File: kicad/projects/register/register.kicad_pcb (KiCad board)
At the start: 2 copper layers, 215.9 x 129.5 mm, 21 parts, among them J1 LEFT IN, J10 RIGHT LEDS, J2 LEFT OUT, J3 LEFT CONTENT, J4 BUS, J5 LEFT LEDS, J6 BACKPLANE, J7 RIGHT IN, J8 RIGHT OUT, J9 RIGHT CONTENT, U1 74HCT377, U2 74HCT245, U3 74HCT04, U4 74HCT377, U5 74HCT245

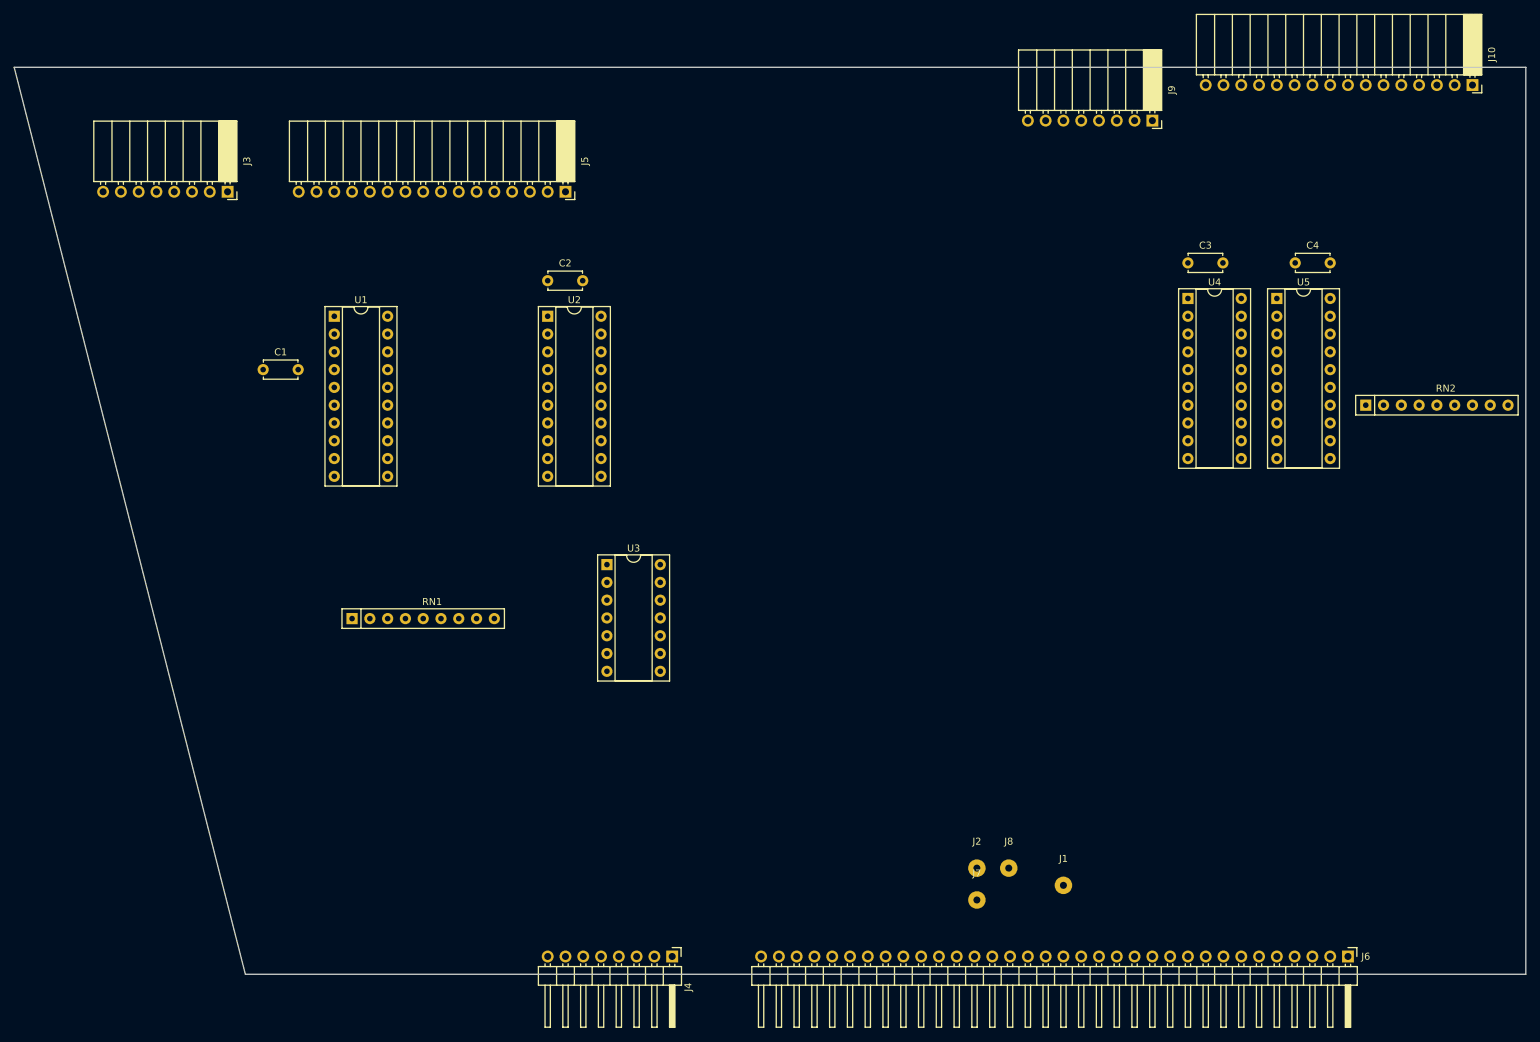
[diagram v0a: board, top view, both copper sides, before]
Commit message: Add start of control unit in kicad. Start routing register PCB, need to make traces thinner...
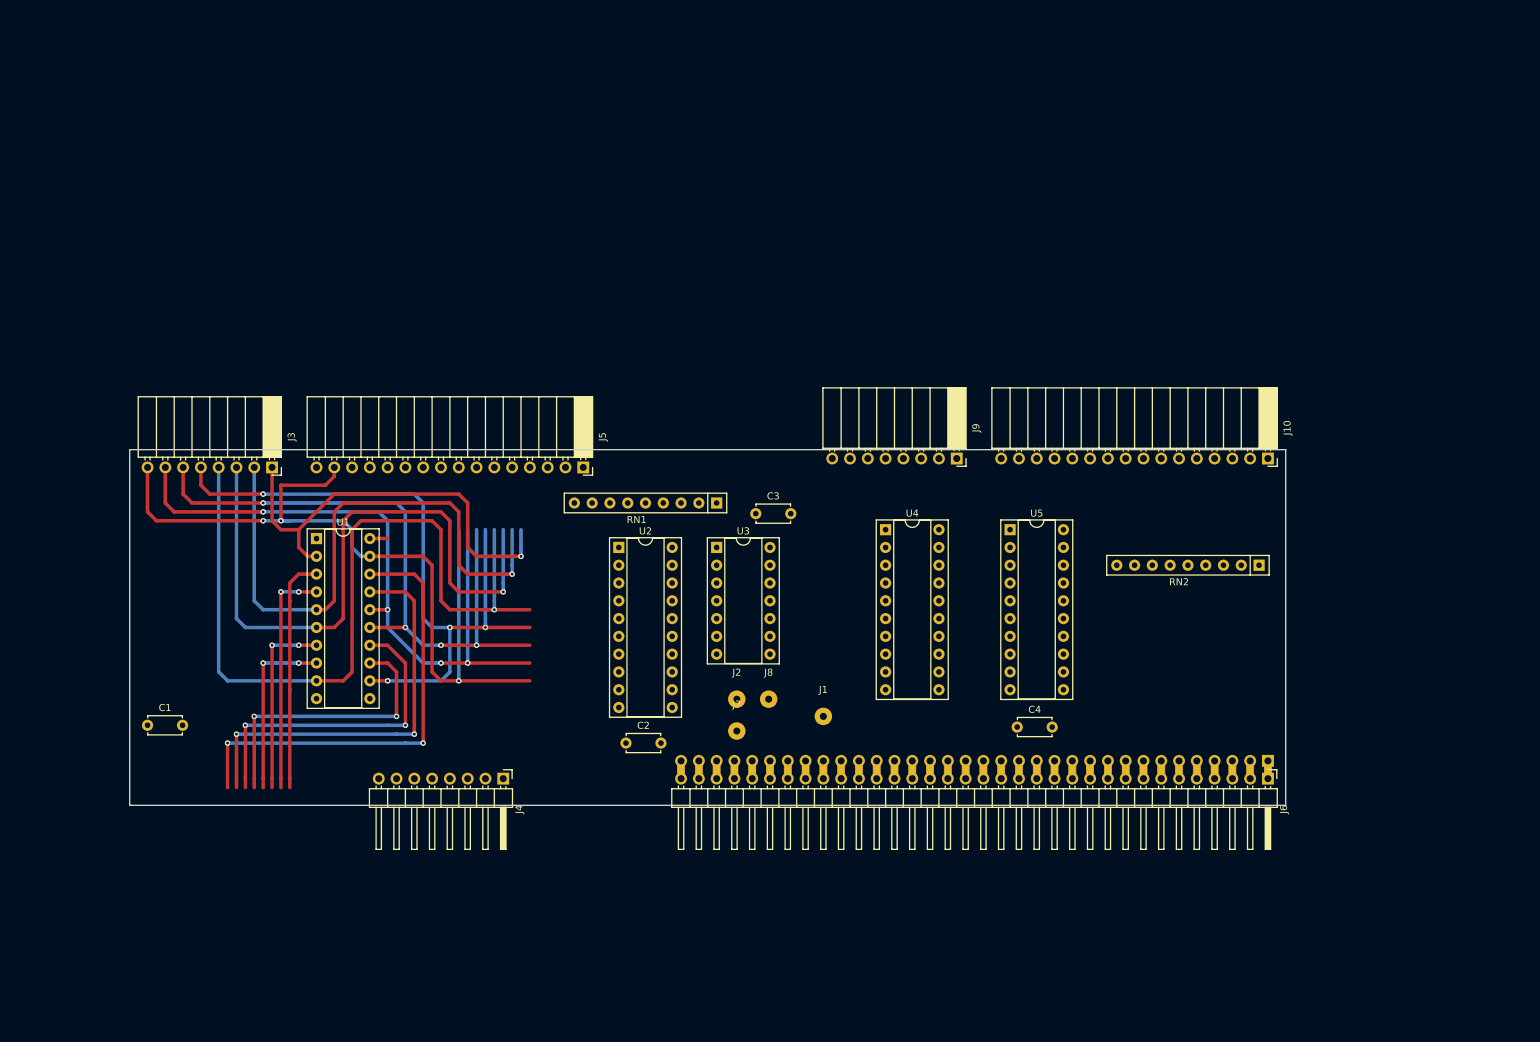
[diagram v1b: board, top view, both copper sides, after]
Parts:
- J6: footprint Connector_PinHeader_2.54mm:PinHeader_1x34_P2.54mm_Horizontal -> eight-bit-computer:backplane-connector
- moved C4 77.3 mm to (183.9, 114.6)
- moved C3 71.4 mm to (146.6, 84.1)
- moved C2 67.0 mm to (128.0, 116.8)
- moved J10 60.8 mm to (219.7, 76.2)
- moved J9 55.8 mm to (175.3, 76.2)
- moved RN1 54.6 mm to (141.0, 82.5), turned to 180 degrees
- moved U4 54.4 mm to (165.1, 86.4)
- moved C1 53.4 mm to (59.7, 114.3)
- moved U5 50.4 mm to (182.9, 86.4)
- moved J1 41.9 mm to (156.2, 113.0)
- moved J2 41.9 mm to (143.8, 110.6)
- moved J7 41.9 mm to (143.8, 115.1)
- moved J8 41.9 mm to (148.4, 110.6)
- moved J3 39.9 mm to (77.5, 77.5)
- moved J5 39.5 mm to (121.9, 77.5)
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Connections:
- net Net-(J6-Pad33) renamed /D_CLK
- J6 pad 30: GND -> Net-(J6-Pad30)
- J6 pad 32: Net-(J6-Pad32) -> GND
- J6 pad 34: (no net) -> Net-(J6-Pad34)
- U3 pad 10: (no net) -> Net-(U3-Pad10)
- U3 pad 11: (no net) -> GND
- U3 pad 12: (no net) -> Net-(U3-Pad12)
- U3 pad 13: (no net) -> GND
- U3 pad 14: (no net) -> VCC
- U3 pad 7: (no net) -> GND
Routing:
- net Net-(J3-Pad8): track 0.00 -> 118.7 mm, vias 0 -> 3
- net Net-(J3-Pad4): track 0.00 -> 118.2 mm, vias 0 -> 1
- net Net-(J3-Pad5): track 0.00 -> 99.9 mm, vias 0 -> 4
- net Net-(J3-Pad7): track 0.00 -> 97.1 mm, vias 0 -> 4
- net Net-(J3-Pad3): track 0.00 -> 94.1 mm, vias 0 -> 1
- net Net-(J3-Pad6): track 0.00 -> 93.5 mm, vias 0 -> 4
- net Net-(J3-Pad2): track 0.00 -> 85.2 mm, vias 0 -> 1
- net /BUS_7: track 0.00 -> 65.3 mm, vias 0 -> 2
- net Net-(J3-Pad1): track 0.00 -> 62.6 mm, vias 0 -> 1
- net /BUS_6: track 0.00 -> 58.9 mm, vias 0 -> 2
- net /BUS_5: track 0.00 -> 46.8 mm, vias 0 -> 2
- net /BUS_4: track 0.00 -> 41.2 mm, vias 0 -> 2
- net /BUS_0: track 0.00 -> 33.5 mm
- net /BUS_1: track 0.00 -> 33.0 mm, vias 0 -> 2
- net /BUS_2: track 0.00 -> 26.7 mm, vias 0 -> 2
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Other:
- board size 215.9 x 129.5 mm -> 165.1 x 50.8 mm
- net class Default: clearance 0.2 -> 0.127; trace_width 0.25 -> 0.254
- rule trace_clearance: 0.2 -> 0.127

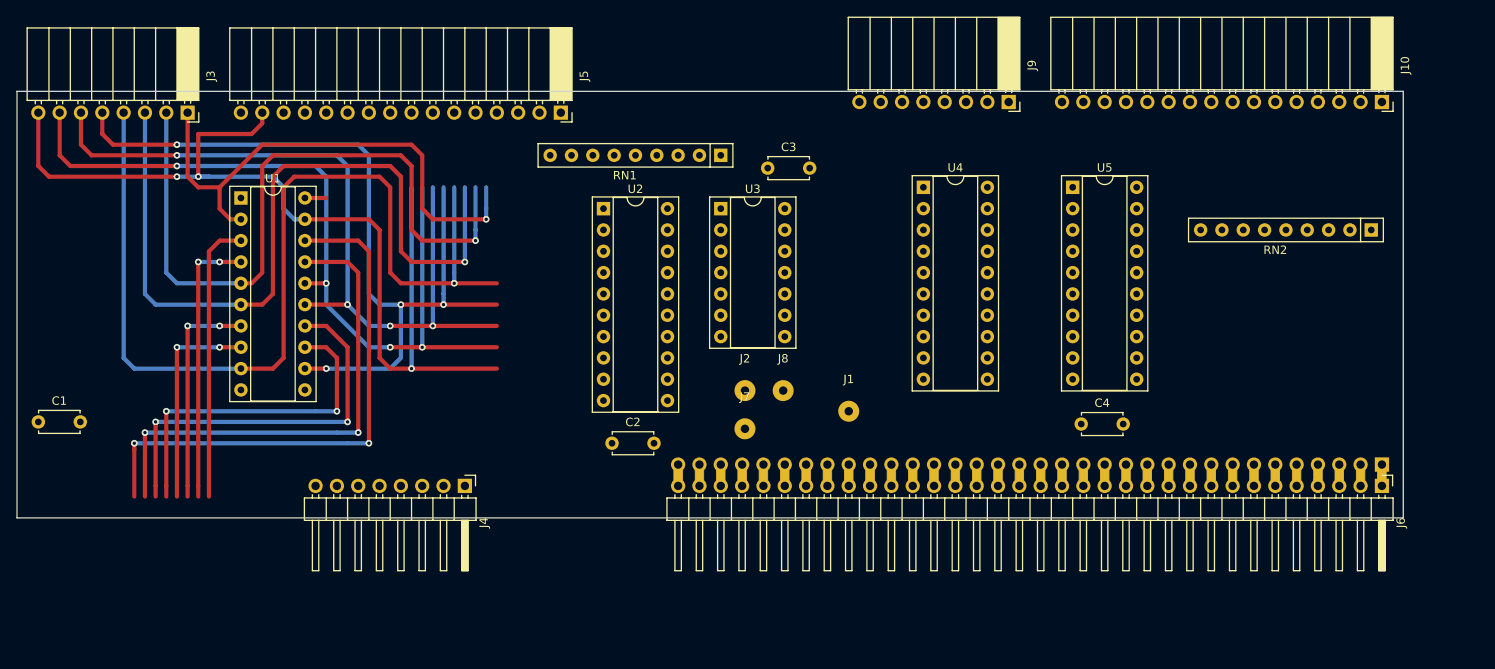
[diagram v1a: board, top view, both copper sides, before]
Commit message: First version of register pcb. Ground and power planes giving poor results.
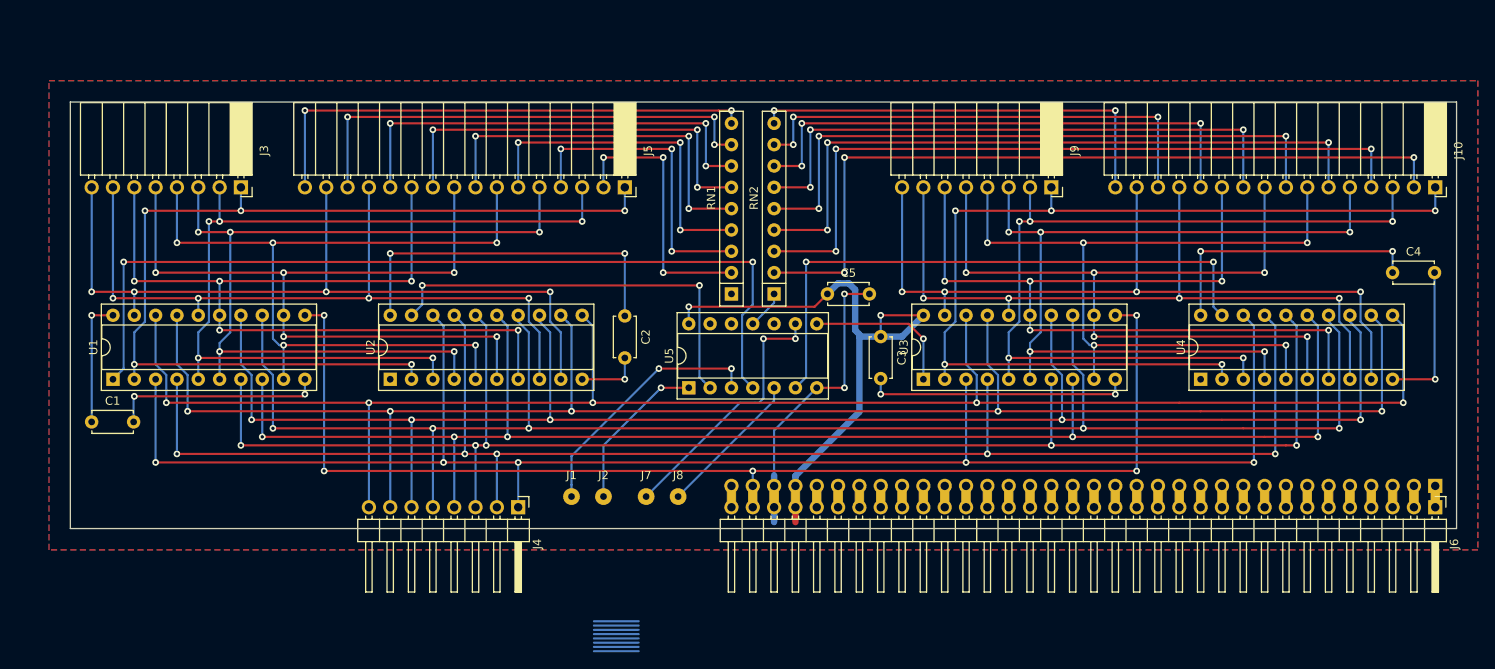
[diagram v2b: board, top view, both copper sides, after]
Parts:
- removed the U3 at (141.0, 88.9)
- added C5: 100nF, Capacitor_THT:C_Disc_D4.7mm_W2.5mm_P5.00mm, F.Cu at (153.7, 99.1)
- added U5: 74HCT04, Package_DIP:DIP-14_W7.62mm_Socket, F.Cu at (137.2, 110.2)
- J1, J2, J7, J8: footprint Connector_Wire:SolderWirePad_1x01_Drill1mm -> Connector_Wire:SolderWirePad_1x01_Drill0.8mm
- moved RN2 71.5 mm to (147.3, 99.1), turned to 90 degrees
- moved C4 41.2 mm to (221.0, 96.5)
- moved J1 34.5 mm to (123.2, 123.2)
- moved U2 32.5 mm to (101.6, 109.2), turned to 90 degrees
- moved U4 27.5 mm to (198.1, 109.2), turned to 90 degrees
- moved U1 26.4 mm to (68.6, 109.2), turned to 90 degrees
- moved C3 24.2 mm to (160.0, 104.1), turned to 270 degrees
- moved U3 22.9 mm to (165.1, 109.2), turned to 90 degrees
- moved J2 21.1 mm to (127.0, 123.2)
- moved J8 17.8 mm to (135.9, 123.2)
- moved RN1 16.6 mm to (142.2, 99.1), turned to 90 degrees
- moved C2 15.2 mm to (129.5, 101.7), turned to 270 degrees
- moved J7 14.3 mm to (132.1, 123.2)
- moved J10 12.0 mm to (226.1, 86.4)
- moved J5 11.7 mm to (129.5, 86.4)
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- renumbered U4 to U3, U5 to U4
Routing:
- net /BUS_0: track 33.5 -> 192.1 mm, vias 0 -> 5
- net VCC: track 2.54 -> 159.1 mm, vias 0 -> 7
- net /BUS_1: track 33.0 -> 189.0 mm, vias 2 -> 5
- net /BUS_2: track 26.7 -> 180.9 mm, vias 2 -> 5
- net /BUS_3: track 25.4 -> 177.8 mm, vias 2 -> 5
- net /BUS_4: track 41.2 -> 192.4 mm, vias 2 -> 5
- net /BUS_5: track 46.8 -> 194.4 mm, vias 2 -> 5
- net /BUS_6: track 58.9 -> 201.9 mm, vias 2 -> 5
- net /D_CLK: track 0.00 -> 140.5 mm, vias 0 -> 5
- net /BUS_7: track 65.3 -> 203.5 mm, vias 2 -> 5
- net GND: track 0.00 -> 122.5 mm, vias 0 -> 8
- net Net-(J10-Pad1): track 0.00 -> 118.1 mm, vias 0 -> 5
- net Net-(U1-Pad1): track 0.00 -> 105.5 mm, vias 0 -> 2
- net Net-(J10-Pad11): track 0.00 -> 102.6 mm, vias 0 -> 5
- net Net-(J10-Pad3): track 0.00 -> 102.4 mm, vias 0 -> 5
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- added copper zone on B.Cu, net GND
- added copper zone on F.Cu, net VCC

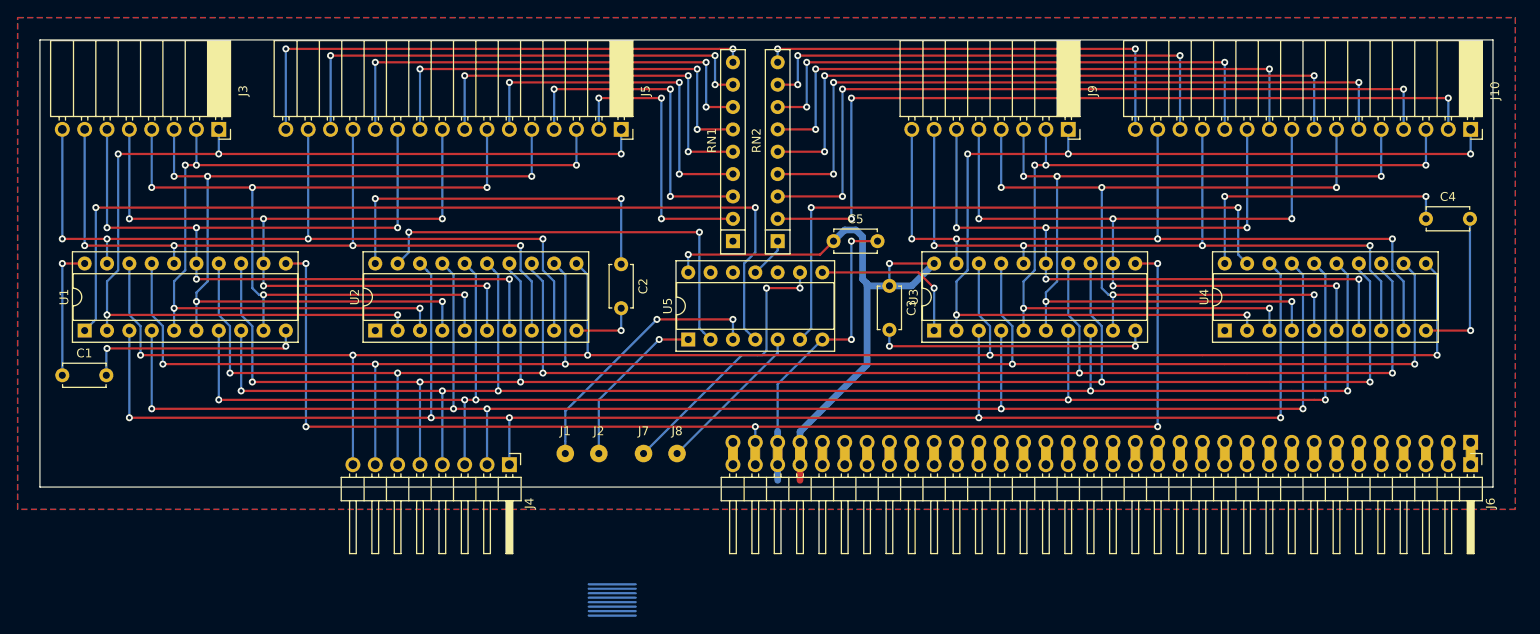
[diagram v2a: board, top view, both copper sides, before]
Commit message: Left register complete.
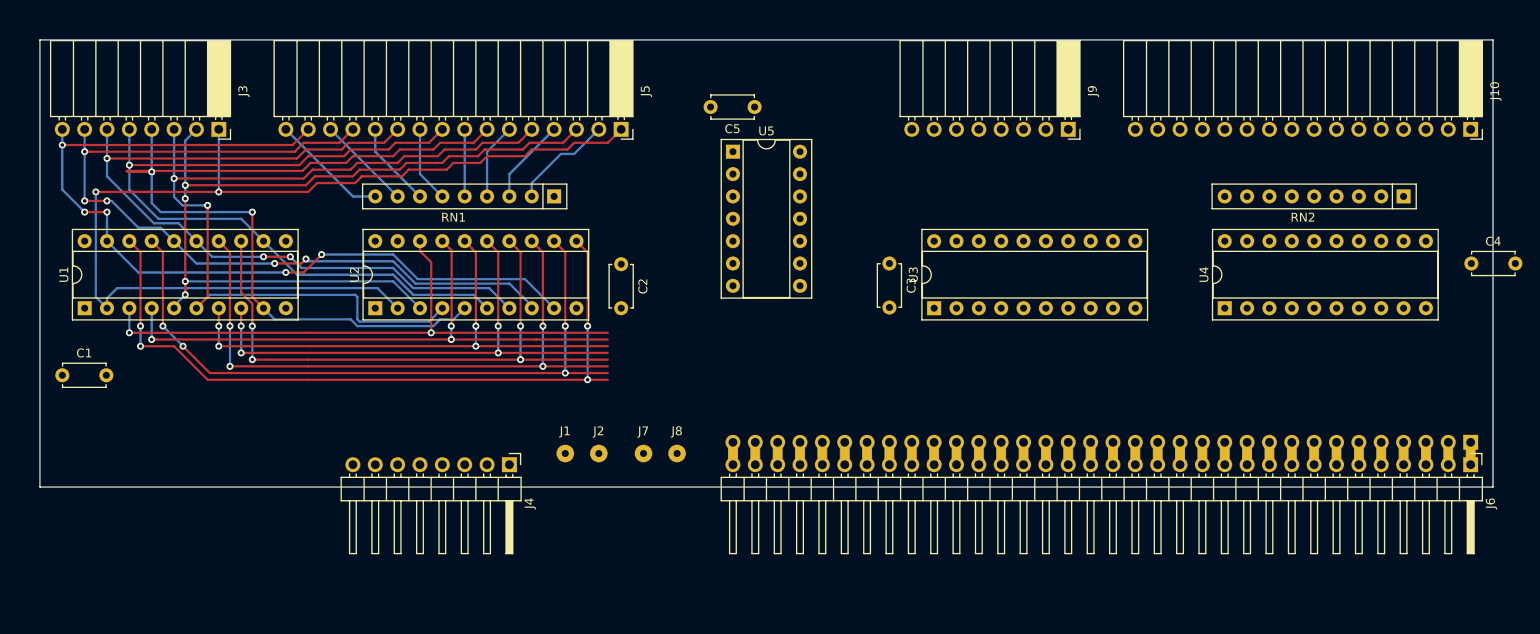
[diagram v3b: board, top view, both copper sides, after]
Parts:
- moved RN2 71.3 mm to (218.4, 94.0), turned to 180 degrees
- moved U5 21.9 mm to (142.2, 88.9), turned to 0 degrees
- moved RN1 20.9 mm to (121.9, 94.0), turned to 180 degrees
- moved C5 17.7 mm to (144.7, 83.8), turned to 180 degrees
- moved C4 7.24 mm to (226.1, 101.6)
- moved C3 2.54 mm to (160.0, 101.6)
- moved U1 2.54 mm to (68.6, 106.7)
- moved U2 2.54 mm to (101.6, 106.7)
- moved U3 2.54 mm to (165.1, 106.7)
- moved U4 2.54 mm to (198.1, 106.7)
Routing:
- net VCC: track 159.1 -> 0.00 mm, vias 7 -> 0
- net /D_CLK: track 140.5 -> 0.00 mm, vias 5 -> 0
- net /BUS_4: track 192.4 -> 68.4 mm, vias 5 -> 4
- net /BUS_0: track 192.1 -> 68.1 mm, vias 5 -> 2
- net /BUS_6: track 201.9 -> 78.4 mm, vias 5 -> 4
- net GND: track 122.5 -> 0.00 mm, vias 8 -> 0
- net /BUS_1: track 189.0 -> 67.0 mm, vias 5 -> 3
- net /BUS_5: track 194.4 -> 72.4 mm, vias 5 -> 4
- net /BUS_7: track 203.5 -> 83.4 mm, vias 5 -> 4
- net /BUS_2: track 180.9 -> 61.0 mm, vias 5 -> 4
- net Net-(J10-Pad1): track 118.1 -> 0.00 mm, vias 5 -> 0
- net /BUS_3: track 177.8 -> 60.0 mm, vias 5 -> 4
- net Net-(U1-Pad1): track 105.5 -> 0.00 mm, vias 2 -> 0
- net Net-(J10-Pad11): track 102.6 -> 0.00 mm, vias 5 -> 0
- net Net-(J10-Pad3): track 102.4 -> 0.00 mm, vias 5 -> 0
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- removed copper zone on B.Cu, net GND
- removed copper zone on F.Cu, net VCC
